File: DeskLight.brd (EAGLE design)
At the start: 44.5 x 58.4 mm, 39 parts, among them IC1 REG1117, J1 Würth Elektronik SD Connector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, T1 MMBT2222, T2 MMBT2222, T3 MJD122, T4 MJD122, T5 MJD122, U1 ESP32-WROOM-32D, U2 CH340C

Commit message: .
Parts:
- IC1: device burr-brown:SOT223 -> burr-brown_:SOT223

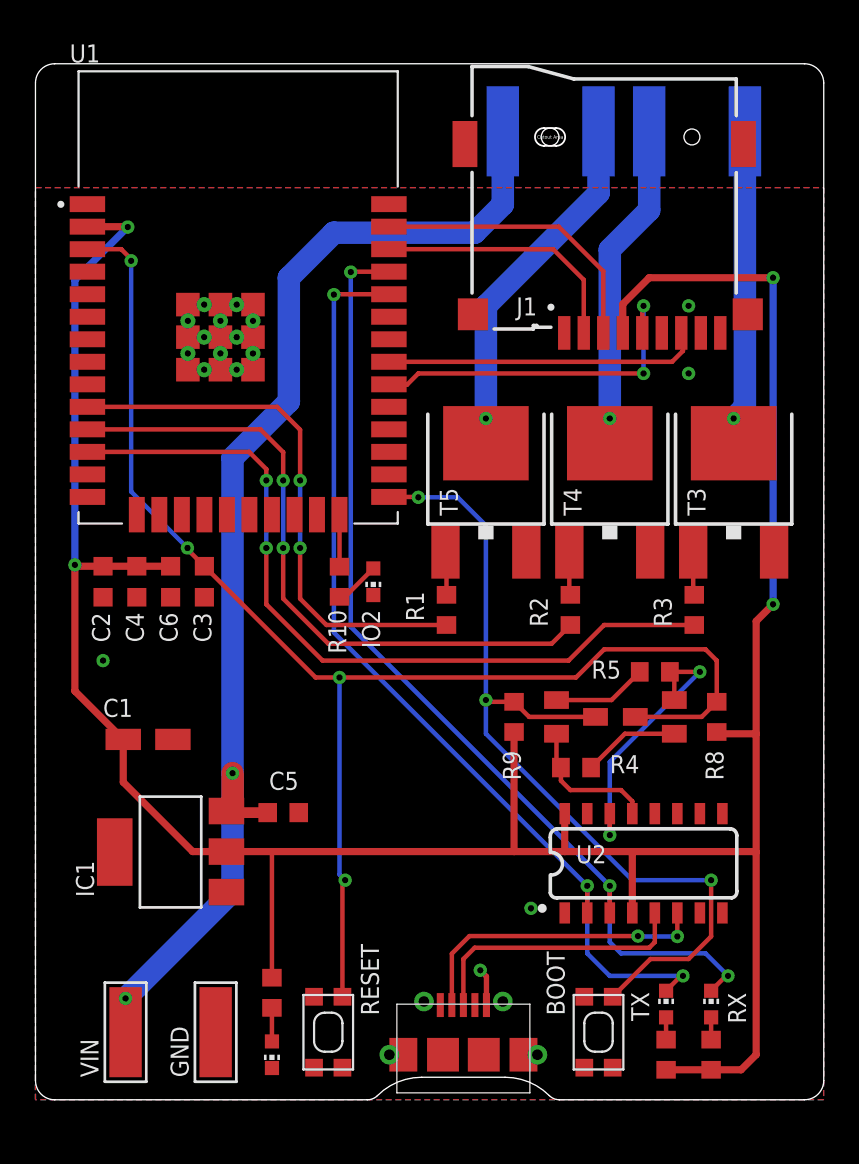
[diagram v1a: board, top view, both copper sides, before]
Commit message: new version with small size and for addressable led strips
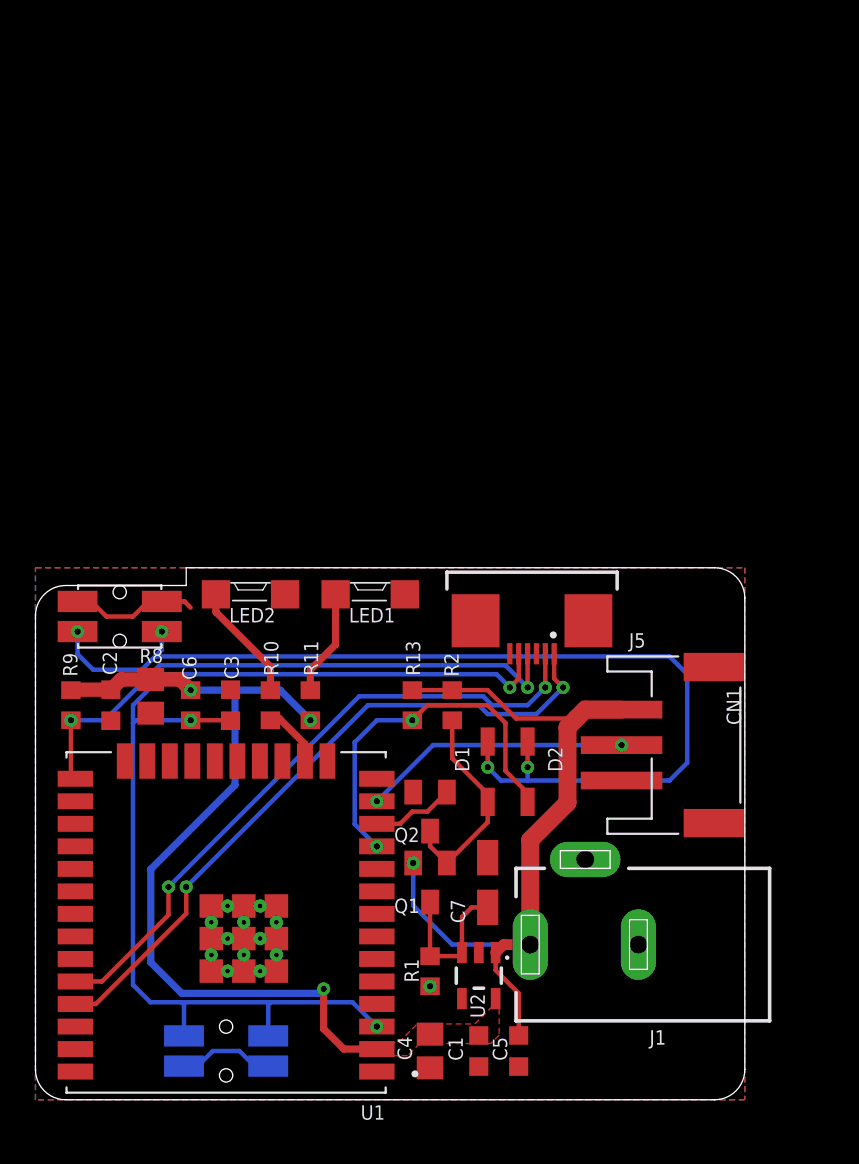
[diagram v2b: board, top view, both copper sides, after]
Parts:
- removed +12V, BLUE, GND, GREEN, VIN: LEDPAD, wirepad:5-1,8
- removed BOOT, RESET: KMR2, adafruit:KMR2
- removed IC1: REG1117, burr-brown_:SOT223
- removed IO2, TX: RED, led:CHIP-LED0603
- removed R3, R4, R5: 10k, rcl:R0603
- removed R6, R7: 1k, rcl:R0603
- removed RED: LEDPAP, wirepad:5-1,8
- removed RX: BLUE, led:CHIP-LED0603
- removed T1, T2: MMBT2222, transistor:SOT23-BEC
- removed T3, T4, T5: MJD122, transistor-neu-to92:DPAK
- removed USB: MICRO-USB-47589-0001, con-molex-usb:47589-0001
- added C7: 1uF, rcl:CT3216
- added CN1: (no value), adafruit:JSTPH3
- added D1, D2: (no value), semicon-smd-ipc:SOD123
- added J5: 68710614022, WR-FPC:68710614022
- added LED2: RED, led:MICRO-SIDELED
- added Q1: BSS84, transistor-small-signal:SOT23
- added Q2: BSS138, transistor-small-signal:SOT23
- added R13: 100k, rcl:R0603
- added U$1, U$67: YD-3414, YD-3414:YD-3414
- C1: value 22uF -> 1uF; device rcl:CT3216 -> rcl:C0603K
- C4: value 0.1uF -> 10uF; device rcl:C0603K -> rcl:C0805
- C5: value 0.1uF -> 1uF
- C6: device rcl:C0603K -> rcl:C0805
- J1: value Würth Elektronik SD Connector 693071020811 -> DCJ0202; device 693071030811_Eagle_WR-CRD_rev20b:693071020811 -> con-jack:DCJ0202
- LED1: device led:CHIP-LED0603 -> led:MICRO-SIDELED
- R1: value 10k -> 1M
- R2: value 10k -> 100k
- U1: value ESP32-WROOM-32D -> ESP32-WROOM-32U; device ESP32-WROOM-32D:MODULE_ESP32-WROOM-32D -> ESP32-WROOM-32U:XCVR_ESP32-WROOM-32U
- U2: value CH340C -> 3.3V; device SparkFun-IC-Comms:SO016 -> SparkFun-IC-Power:SOT23-5
- moved J1 45.6 mm to (31.0, 8.75), turned to 90 degrees
- moved U1 35.3 mm to (10.8, 10.0), turned to 180 degrees
- moved C4 31.2 mm to (22.2, 2.75)
- moved R8 29.7 mm to (8.75, 22.2), turned to 90 degrees
- moved LED1 26.5 mm to (18.9, 28.5), turned to 90 degrees
- moved C1 25.6 mm to (25.0, 2.75), turned to 270 degrees
- moved R9 25.0 mm to (2.00, 22.2), turned to 90 degrees
- moved R1 20.4 mm to (22.2, 7.25)
- moved C5 18.9 mm to (27.2, 2.75), turned to 270 degrees
- moved R11 16.4 mm to (15.5, 22.2), turned to 270 degrees
- moved U2 11.2 mm to (25.0, 7.00), turned to 180 degrees
- moved R2 8.56 mm to (23.5, 22.2)
- moved R10 7.98 mm to (13.2, 22.2), turned to 270 degrees
- moved C3 7.11 mm to (11.0, 22.2), turned to 90 degrees
- moved C2 6.97 mm to (4.25, 22.2)
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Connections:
- removed net B: BLUE.1, T5.4
- removed net CB: R1.1, U1.10
- removed net CG: R3.1, U1.12
- removed net CR: R2.1, U1.11
- removed net DTR: R4.1, T1.E, U2.13
- removed net ESP_EN: C3.1, R8.1, RESET.2, T2.C, U1.3
- removed net G: GREEN.1, T3.4
- removed net GPIO0: BOOT.2, R9.1, T1.C, U1.25
- removed net MISO: J1.7, U1.31
- removed net MOSI: J1.3, U1.37
- removed net N$10: R10.2, U1.24
- removed net N$12: U2.6, USB.2
- removed net N$3: R5.2, T1.B
- removed net N$4: R4.2, T2.B
- removed net N$5: R6.1, RX.A
- removed net N$6: R7.1, TX.A
- removed net N$7: R3.2, T3.1
- removed net R: RED.1, T4.4
- removed net RTS: R5.1, T2.E, U2.14
- removed net RXI: RX.C, U1.35, U2.3
- removed net SCLK: J1.5, U1.30
- removed net SD_CS: J1.2, U1.36
- removed net TXO: TX.C, U1.34, U2.2
- removed net VIN: +12V.1, C5.1, IC1.3, VIN.1
- new net +5V: C5.1, CN1.1, J1.1, Q1.2, R13.1, R2.2, U2.1
- new net BOOT: J5.4, R9.1, U1.25
- new net ESP32_RX: J5.2, U1.34
- new net ESP32_TX: J5.1, U1.35
- new net LED_CTRL: CN1.2, U1.13
- new net POWER_CTRL: Q2.1, U1.12
- new net POWER_EN: C7.+, Q1.3, R1.2, U2.3
- new net POWER_SENSE: D2.2, R13.2, U1.11
- new net RESET: C3.1, J5.5, R8.1, U$1.P$1, U$1.P$2, U1.3
- net +3V3: now also C1.1, U2.5; no longer C1.+, IC1.2, J1.4, R6.2, R7.2, U2.16, U2.4
- net GND: now also C1.2, C7.-, CN1.3, J1.2, J1.3, J5.6, J5.Z1, J5.Z2, LED2.C, Q2.2, R1.1, U$1.P$3, U$1.P$4, U$67.P$3, U$67.P$4, U1.G.1, U1.G.10, U1.G.11, U1.G.12, U1.G.13, U1.G.14, U1.G.15, U1.G.16, U1.G.17, U1.G.18, U1.G.19, U1.G.2, U1.G.20, U1.G.21, U1.G.22, U1.G.4, U1.G.5, U1.G.6, U1.G.7, U1.G.8, U1.G.9, U2.2; no longer BOOT.1, BOOT.3, C1.-, GND.1, IC1.1, IO2.C, J1.6, RESET.1, RESET.3, T3.3, T4.3, T5.3, U1.39_1, U1.39_10, U1.39_11, U1.39_12, U1.39_13, U1.39_14, U1.39_15, U1.39_16, U1.39_17, U1.39_18, U1.39_19, U1.39_2, U1.39_20, U1.39_21, U1.39_3, U1.39_4, U1.39_5, U1.39_6, U1.39_7, U1.39_8, U1.39_9, U2.1, USB.5
- net N$1: now also D1.2, Q1.1, Q2.3, R2.1; no longer R1.2, T5.1
- net N$11: now also D1.1, D2.1, U$67.P$1, U$67.P$2; no longer U2.5, USB.3
- net N$13: now also LED2.A; no longer IO2.A
- net N$2: now also R10.2, U1.16; no longer R2.2, T4.1
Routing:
- net +3V3: track 160.8 -> 48.3 mm, vias 4 -> 3
- net ESP_EN: track 79.6 -> 0.00 mm, vias 4 -> 0
- net VIN: track 68.9 -> 0.00 mm, vias 2 -> 0
- net RESET: track 0.00 -> 64.4 mm, vias 0 -> 3
- net RXI: track 56.3 -> 0.00 mm, vias 3 -> 0
- net TXO: track 54.9 -> 0.00 mm, vias 3 -> 0
- net GPIO0: track 50.7 -> 0.00 mm, vias 3 -> 0
- net CG: track 44.4 -> 0.00 mm, vias 2 -> 0
- net +5V: track 0.00 -> 43.8 mm, vias 0 -> 1
- net N$11: track 15.4 -> 58.9 mm, vias 0 -> 4
- net ESP32_TX: track 0.00 -> 38.3 mm, vias 0 -> 2
- net CR: track 37.5 -> 0.00 mm, vias 2 -> 0
- net ESP32_RX: track 0.00 -> 36.6 mm, vias 0 -> 2
- net BOOT: track 0.00 -> 32.9 mm, vias 0 -> 2
- net CB: track 30.9 -> 0.00 mm, vias 2 -> 0
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- added copper zone on layer 1, net +3V3
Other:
- board size 44.5 x 58.4 mm -> 40 x 30 mm
- board text removed: "BOOT"
- board text removed: "RESET"

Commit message: reviewed
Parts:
- C1, C2, C3, C5: device rcl:C0603K -> rcl:C0603
- moved R1 0.25 mm to (22.2, 7.00)
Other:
- outline, holes or cut-outs redrawn

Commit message: .
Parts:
- moved LED1 0.25 mm to (18.9, 28.8)
- moved LED2 0.25 mm to (12.1, 28.8)
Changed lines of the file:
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@@
 <?xml version="1.0" encoding="utf-8"?>
 <!DOCTYPE eagle SYSTEM "eagle.dtd">
-<eagle version="9.4.0">
+<eagle version="9.6.2">
 <drawing>
 <settings>
-<setting alwaysvectorfont="no"/>
+<setting alwaysvectorfont="yes"/>
 <setting verticaltext="up"/>
 </settings>
@@
 <attribute name="VALUE" x="24.575" y="20.405" size="1.27" layer="27" rot="R270"/>
 </element>
-<element name="LED2" library="led" library_urn="urn:adsk.eagle:library:259" package="MICRO-SIDELED" package3d_urn="urn:adsk.eagle:package:15815/1" override_package3d_urn="urn:adsk.eagle:package:27501285/2" override_package_urn="urn:adsk.eagle:footprint:15669/1" value="RED" x="12.125" y="28.5" smashed="yes" rot="R90">
-<attribute name="NAME" x="13.53" y="27.73" size="0.8128" layer="25" ratio="12" rot="R180"/>
-<attribute name="POPULARITY" value="0" x="56.575" y="45.01" size="1.778" layer="27" rot="R90" display="off"/>
-<attribute name="VALUE" x="14.03" y="31.04" size="0.8128" layer="27" ratio="12" rot="R180"/>
+<element name="LED2" library="led" library_urn="urn:adsk.eagle:library:259" package="MICRO-SIDELED" package3d_urn="urn:adsk.eagle:package:15815/1" override_package3d_urn="urn:adsk.eagle:package:27501285/2" override_package_urn="urn:adsk.eagle:footprint:15669/1" value="RED" x="12.125" y="28.75" smashed="yes" rot="R90">
+<attribute name="NAME" x="13.53" y="27.98" size="0.8128" layer="25" ratio="12" rot="R180"/>
+<attribute name="POPULARITY" value="0" x="56.575" y="45.26" size="1.778" layer="27" rot="R90" display="off"/>
+<attribute name="VALUE" x="14.03" y="31.29" size="0.8128" layer="27" ratio="12" rot="R180"/>
 </element>
 <element name="J1" library="con-jack" library_urn="urn:adsk.eagle:library:154" package="DCJ0202" package3d_urn="urn:adsk.eagle:package:7491/1" override_package3d_urn="urn:adsk.eagle:package:27501288/3" override_package_urn="urn:adsk.eagle:footprint:7486/1" value="DCJ0202" x="31" y="8.75" smashed="yes" rot="R90">
@@
 <attribute name="WORKING-VOLTAGE" value="50V(AC)" x="-2.48" y="65.6" size="1.778" layer="27" rot="R180" display="off"/>
 </element>
-<element name="LED1" library="led" library_urn="urn:adsk.eagle:library:259" package="MICRO-SIDELED" package3d_urn="urn:adsk.eagle:package:15815/1" override_package3d_urn="urn:adsk.eagle:package:27501287/2" override_package_urn="urn:adsk.eagle:footprint:15669/1" value="RED" x="18.875" y="28.5" smashed="yes" rot="R90">
-<attribute name="NAME" x="20.28" y="27.73" size="0.8128" layer="25" ratio="12" rot="R180"/>
-<attribute name="POPULARITY" value="0" x="56.975" y="50.09" size="1.778" layer="27" rot="R90" display="off"/>
-<attribute name="VALUE" x="20.78" y="31.04" size="0.8128" layer="27" ratio="12" rot="R180"/>
+<element name="LED1" library="led" library_urn="urn:adsk.eagle:library:259" package="MICRO-SIDELED" package3d_urn="urn:adsk.eagle:package:15815/1" override_package3d_urn="urn:adsk.eagle:package:27501287/2" override_package_urn="urn:adsk.eagle:footprint:15669/1" value="RED" x="18.875" y="28.75" smashed="yes" rot="R90">
+<attribute name="NAME" x="20.28" y="27.98" size="0.8128" layer="25" ratio="12" rot="R180"/>
+<attribute name="POPULARITY" value="0" x="56.975" y="50.34" size="1.778" layer="27" rot="R90" display="off"/>
+<attribute name="VALUE" x="20.78" y="31.29" size="0.8128" layer="27" ratio="12" rot="R180"/>
 </element>
 <element name="Q1" library="transistor-small-signal" library_urn="urn:adsk.eagle:library:401" package="SOT23" package3d_urn="urn:adsk.eagle:package:28738/2" value="BSS84" x="22.25" y="12.25" smashed="yes" rot="R180">
@@
 <contactref element="LED2" pad="A"/>
 <wire x1="13.25" y1="24.425" x2="10.175" y2="27.5" width="0.4064" layer="1"/>
-<wire x1="10.175" y1="28.5" x2="10.175" y2="27.5" width="0.4064" layer="1"/>
+<wire x1="10.175" y1="28.75" x2="10.175" y2="27.5" width="0.4064" layer="1"/>
 <wire x1="13.25" y1="24.425" x2="13.25" y2="23.1" width="0.4064" layer="1"/>
 </signal>
@@
 <contactref element="R11" pad="1"/>
 <contactref element="LED1" pad="A"/>
-<wire x1="16.925" y1="28.5" x2="16.925" y2="25.675" width="0.4064" layer="1"/>
+<wire x1="16.925" y1="28.75" x2="16.925" y2="25.675" width="0.4064" layer="1"/>
 <wire x1="16.925" y1="25.675" x2="15.5" y2="24.25" width="0.4064" layer="1"/>
 <wire x1="15.5" y1="24.25" x2="15.5" y2="23.1" width="0.4064" layer="1"/>
@@
 <contactref element="U2" pad="1"/>
 <contactref element="CN1" pad="1"/>
-<wire x1="27.25" y1="3.6" x2="27.25" y2="6" width="0.254" layer="1"/>
-<wire x1="25.95" y1="7.3" x2="25.95" y2="8.3001" width="0.254" layer="1"/>
-<wire x1="27.25" y1="6" x2="25.95" y2="7.3" width="0.254" layer="1"/>
 <wire x1="27.9" y1="8.75" x2="27.9" y2="14.65" width="1.016" layer="1"/>
 <wire x1="27.9" y1="14.65" x2="30" y2="16.75" width="1.016" layer="1"/>
@@
 <wire x1="25.95" y1="8.3001" x2="26.3999" y2="8.75" width="0.6096" layer="1"/>
 <wire x1="26.3999" y1="8.75" x2="27.9" y2="8.75" width="0.6096" layer="1"/>
+<wire x1="27.9" y1="8.75" x2="27.9" y2="4.25" width="0.6096" layer="1"/>
+<wire x1="27.9" y1="4.25" x2="27.25" y2="3.6" width="0.6096" layer="1"/>
 </signal>
 <signal name="POWER_EN">
